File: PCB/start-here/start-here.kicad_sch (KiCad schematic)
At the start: 4 parts, among them J1 RJ45_Hanrun_HR911105A_Horizon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, U1 STM32F439ZITx, U2 LAN8742A, U3 AP7361C-10E

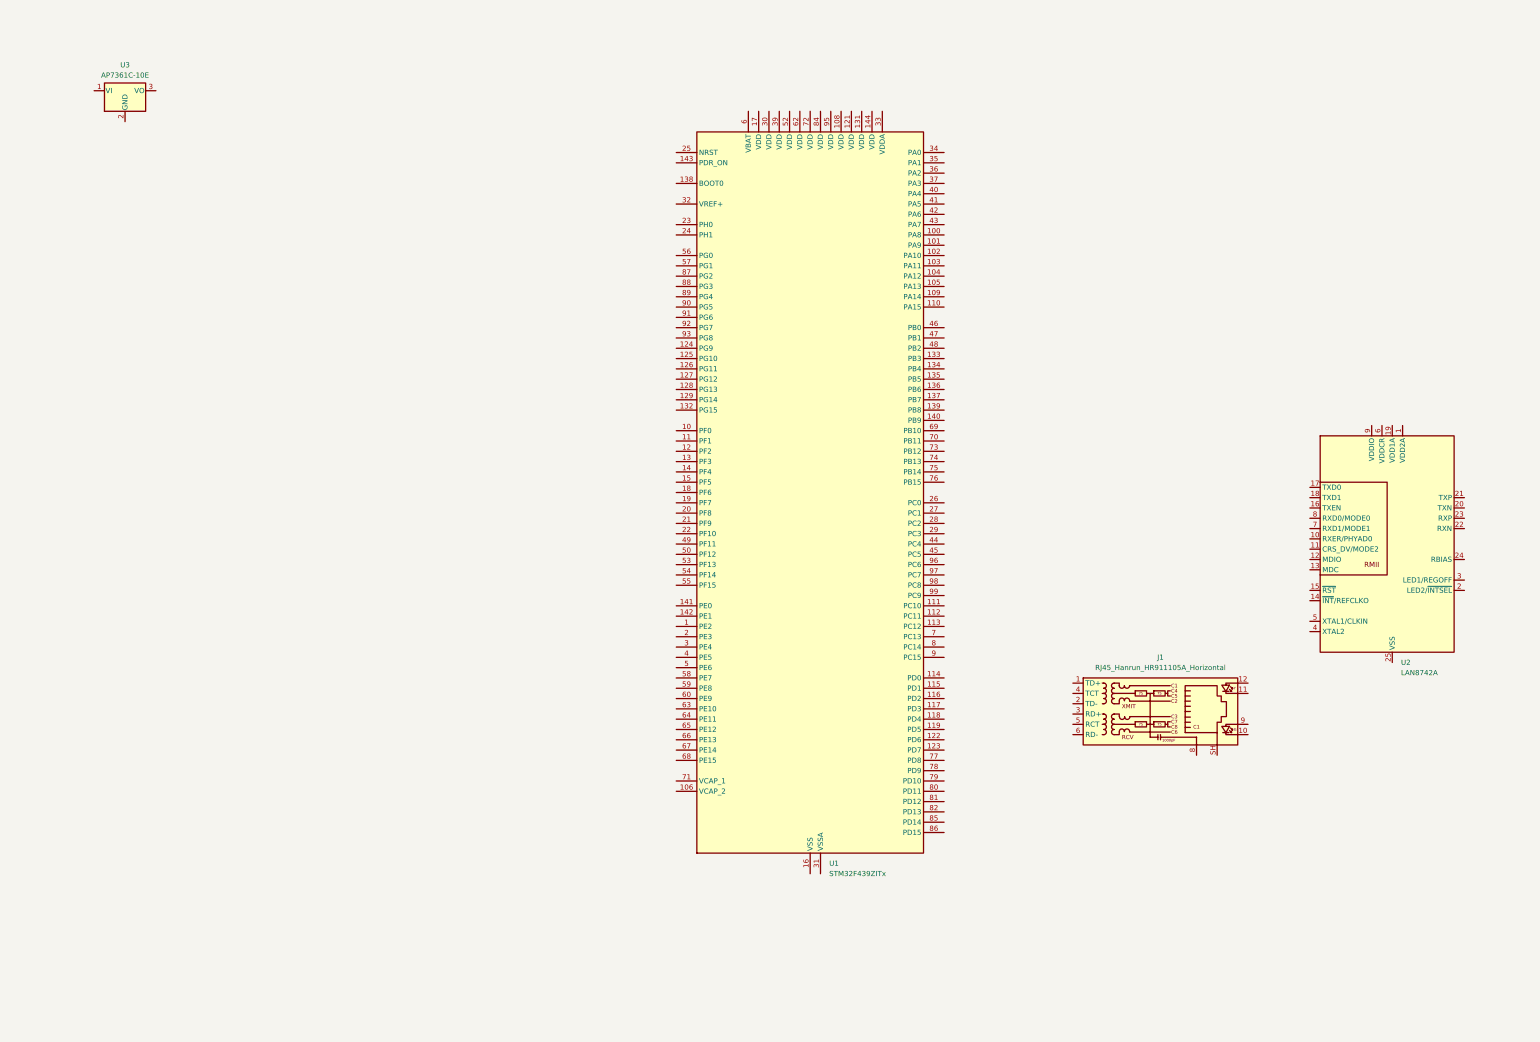
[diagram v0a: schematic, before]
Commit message: Route RMII and update datasheets.md
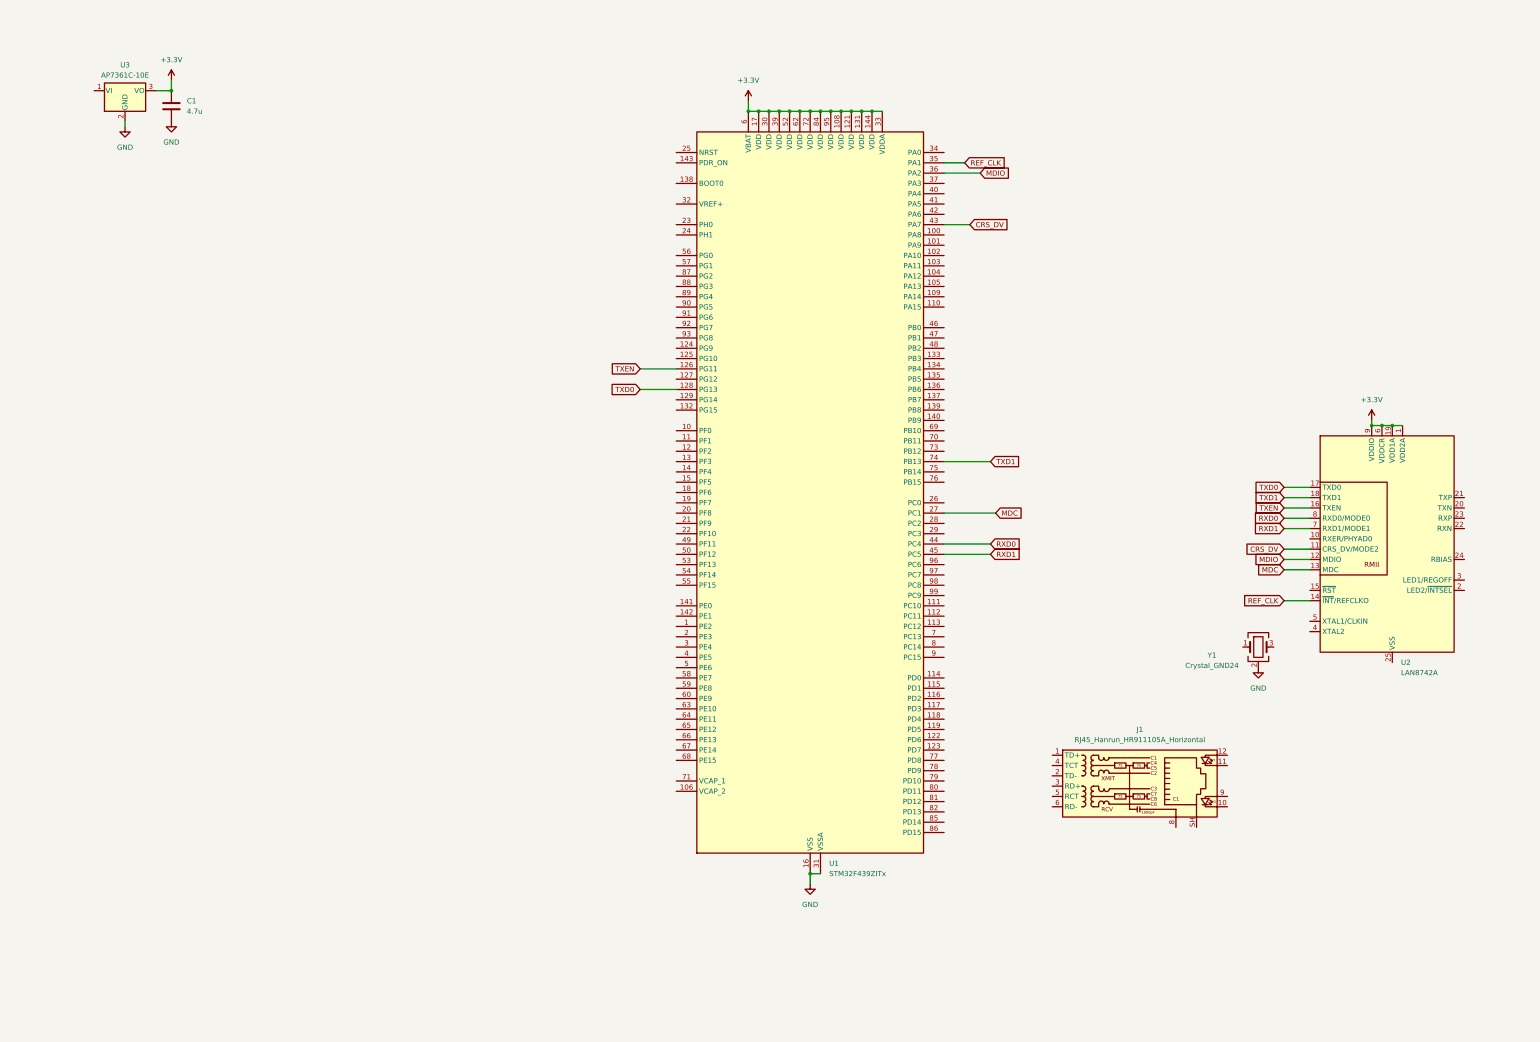
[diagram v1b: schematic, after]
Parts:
- added C1: 4.7u, Capacitor_SMD:C_1206_3216Metric, symbol Device:C
- added Y1: Crystal_GND24, Crystal:Crystal_SMD_3225-4Pin_3.2x2.5mm, symbol Device:Crystal_GND24
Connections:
- net GND: now reaches U3.2 (GND)
- net GND: now also U1.107 (VSS), U1.120 (VSS), U1.130 (VSS), U1.16 (VSS), U1.31 (VSSA), U1.38 (VSS), U1.51 (VSS), U1.61 (VSS), U1.83 (VSS), U1.94 (VSS), C1.2, Y1.2 (G), Y1.4 (G)
- net +3.3V: now reaches U3.3 (VO)
- net +3.3V: now also U1.108 (VDD), U1.121 (VDD), U1.131 (VDD), U1.144 (VDD), U1.17 (VDD), U1.30 (VDD), U1.33 (VDDA), U1.39 (VDD), U1.52 (VDD), U1.6 (VBAT), U1.62 (VDD), U1.72 (VDD), U1.84 (VDD), U1.95 (VDD), U2.1 (VDD2A), U2.19 (VDD1A), U2.6 (VDDCR), U2.9 (VDDIO), C1.1
- net TXEN: now reaches U1.126 (PG11)
- net TXEN: now also U2.16 (TXEN)
- net TXD0: now reaches U1.128 (PG13)
- net TXD0: now also U2.17 (TXD0)
- net MDC: now reaches U1.27 (PC1)
- net MDC: now also U2.13 (MDC)
- net REF_CLK: now reaches U1.35 (PA1)
- net REF_CLK: now also U2.14 (~{INT}/REFCLKO)
- net MDIO: now reaches U1.36 (PA2)
- net MDIO: now also U2.12 (MDIO)
- net CRS_DV: now reaches U1.43 (PA7)
- net CRS_DV: now also U2.11 (CRS_DV/MODE2)
- net RXD0: now reaches U1.44 (PC4)
- net RXD0: now also U2.8 (RXD0/MODE0)
- net RXD1: now reaches U1.45 (PC5)
- net RXD1: now also U2.7 (RXD1/MODE1)
- net TXD1: now reaches U1.74 (PB13)
- net TXD1: now also U2.18 (TXD1)
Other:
- moved on the sheet: J1

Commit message: update schematics
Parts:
- added C2: 15 pF, symbol Device:C
- added C3: 15pF, symbol Device:C
- added R1: 12.1K 1%, symbol Device:R
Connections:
- net +3.3V: now also U2.15 (~{RST})
- net GND: now also J1.8, U2.25 (VSS), C2.2, C3.2, R1.2
- net TXP: now reaches J1.1 (TD+)
- net TXP: now also U2.21 (TXP)
- net TXN: now reaches J1.2 (TD-)
- net TXN: now also U2.20 (TXN)
- net RXP: now reaches J1.3 (RD+)
- net RXP: now also U2.23 (RXP)
- net RXN: now reaches J1.6 (RD-)
- net RXN: now also U2.22 (RXN)
- net at Y1.1: now also U2.5 (XTAL1/CLKIN), C3.1
- net at Y1.3: now also U2.4 (XTAL2), C2.1
- net at U2.24 (RBIAS): now also R1.1
- no-connect marks 0 -> 1
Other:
- moved on the sheet: Y1

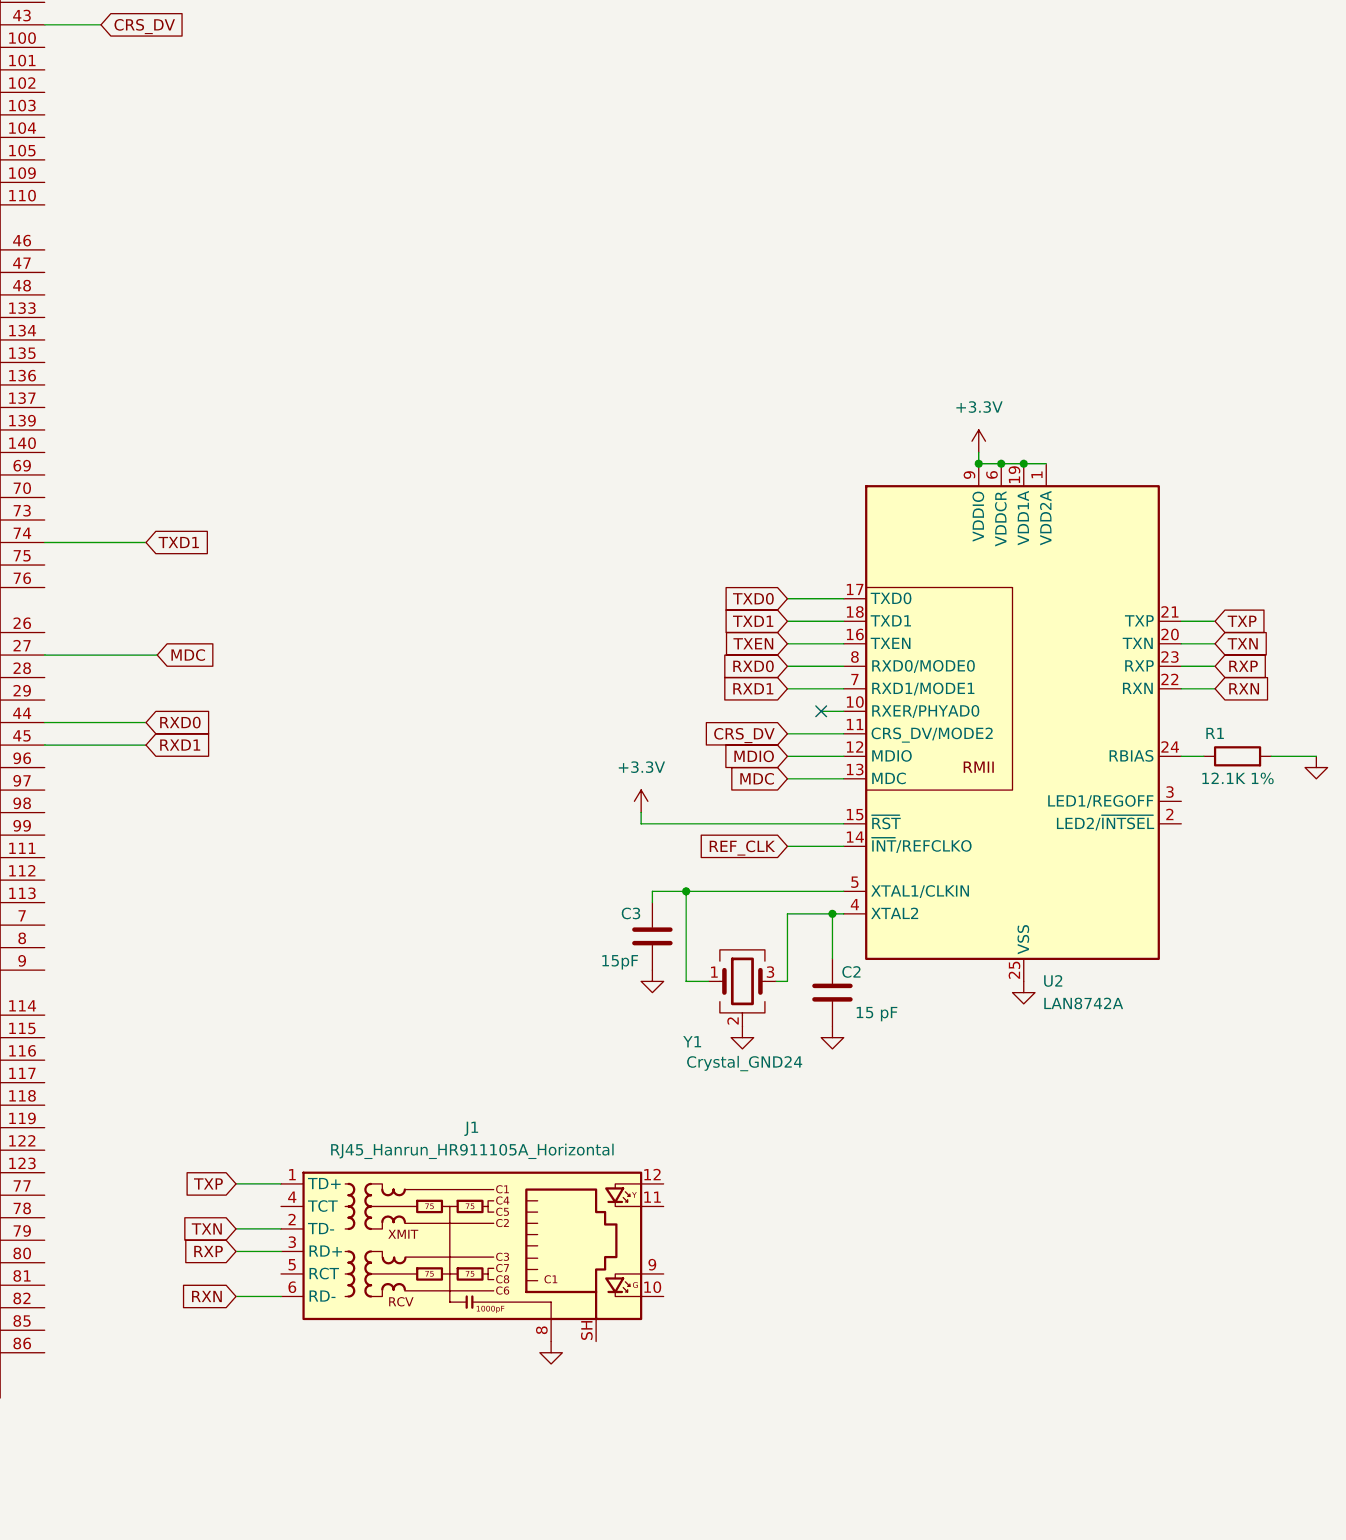
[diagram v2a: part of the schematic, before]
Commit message: update schematics: update power on the PHY, connect LEDs and add ferrite bead
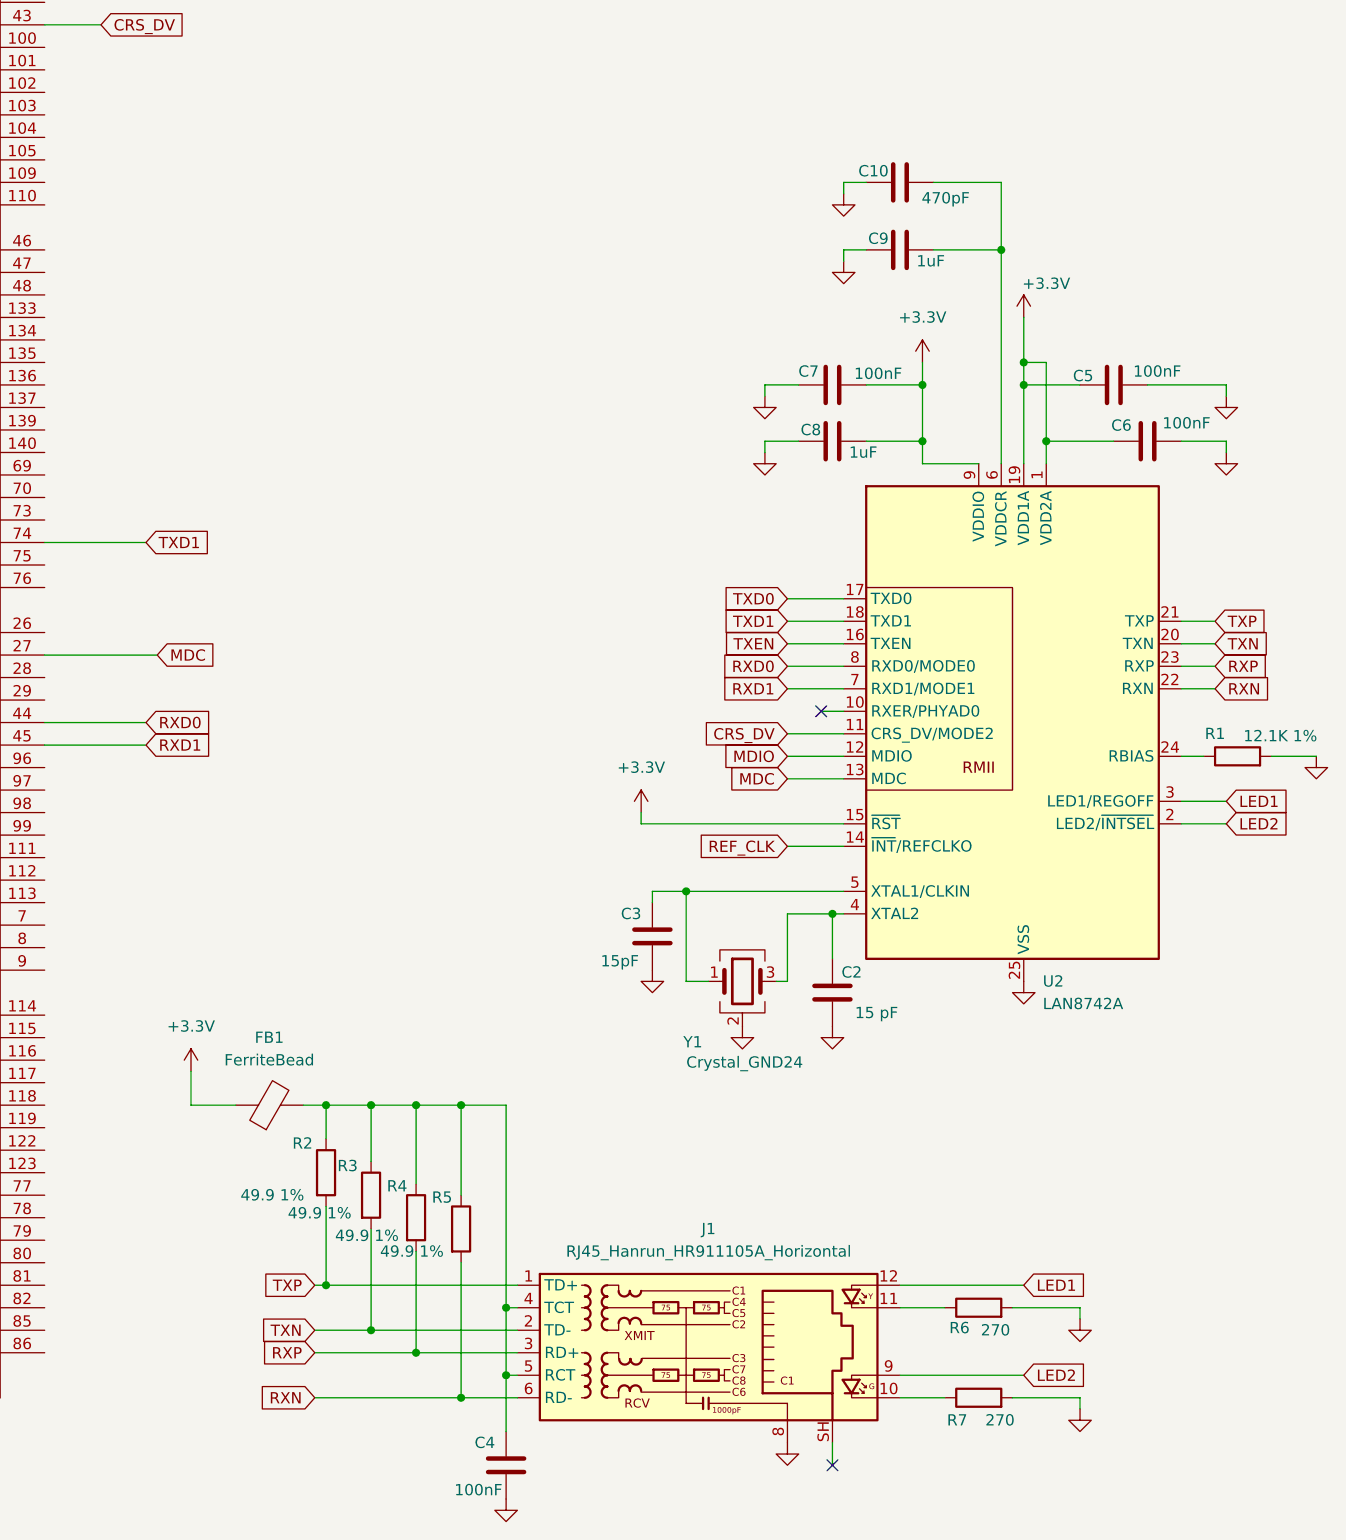
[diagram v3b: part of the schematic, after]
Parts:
- added C10: 470pF, symbol Device:C
- added C4, C5, C6, C7: 100nF, symbol Device:C
- added C8, C9: 1uF, symbol Device:C
- added FB1: FerriteBead, symbol Device:FerriteBead
- added R2, R3, R4, R5: 49.9 1%, symbol Device:R
- added R6, R7: 270, symbol Device:R
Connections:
- net +3.3V: now also C5.1, C6.1, C7.2, C8.2, FB1.1; no longer U2.6 (VDDCR)
- net GND: now also C10.1, C4.2, C5.2, C6.2, C7.1, C8.1, C9.1, R6.2, R7.2
- net RXN: now also R5.2
- net RXP: now also R4.2
- net TXN: now also R3.2
- net TXP: now also R2.2
- net at J1.10: now also R7.1
- net at J1.11: now also R6.1
- net LED1: now reaches J1.12
- net LED1: now also U2.3 (LED1/REGOFF)
- net at J1.4 (TCT): now also J1.5 (RCT), C4.1, FB1.2, R2.1, R3.1, R4.1, R5.1
- net LED2: now reaches J1.9
- net LED2: now also U2.2 (LED2/~{INTSEL})
- new net: C10.2, C9.2, U2.6 (VDDCR)
- no-connect marks 1 -> 2
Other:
- moved on the sheet: J1
